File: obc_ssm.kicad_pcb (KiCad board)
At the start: 4 copper layers, 98 x 84 mm, 31 parts, among them IC1 DS3234, J1 RST_JMP, J2 DEBUG CONN, J3 PROGRAMMING PORT, SW1 SW_RST, U1 SN65HVD230, U2 ATMEGA32M1-MU, U3 SST25VF016B, Y1 8MHz

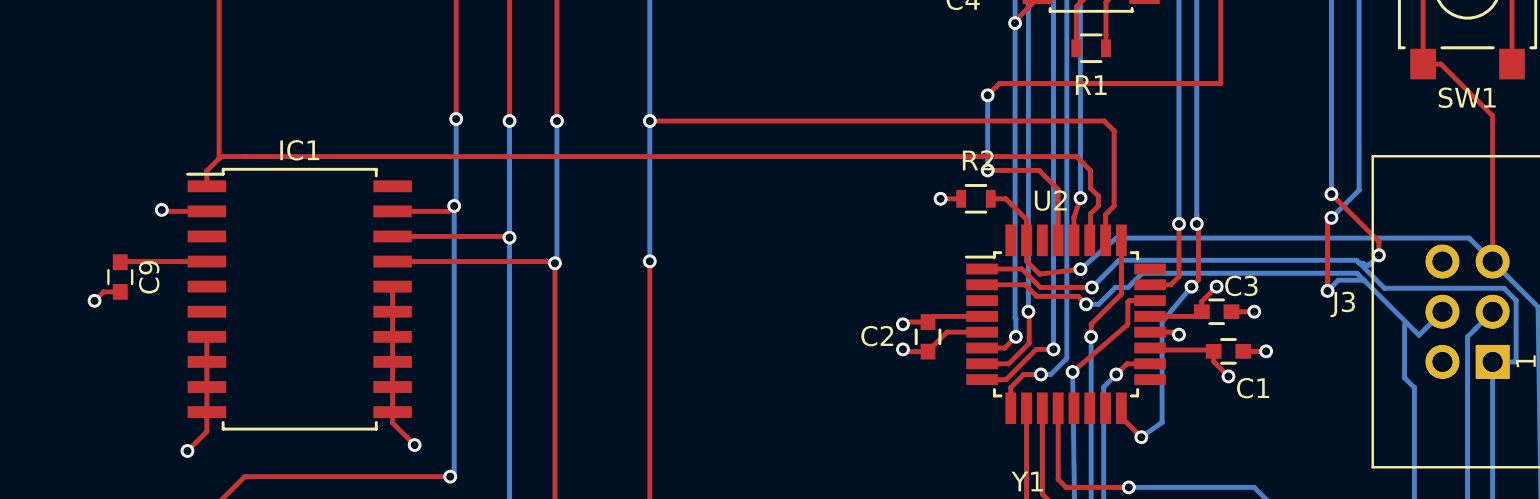
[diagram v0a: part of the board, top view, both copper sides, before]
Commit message: Fix missing connections; DRC check passes
Please review
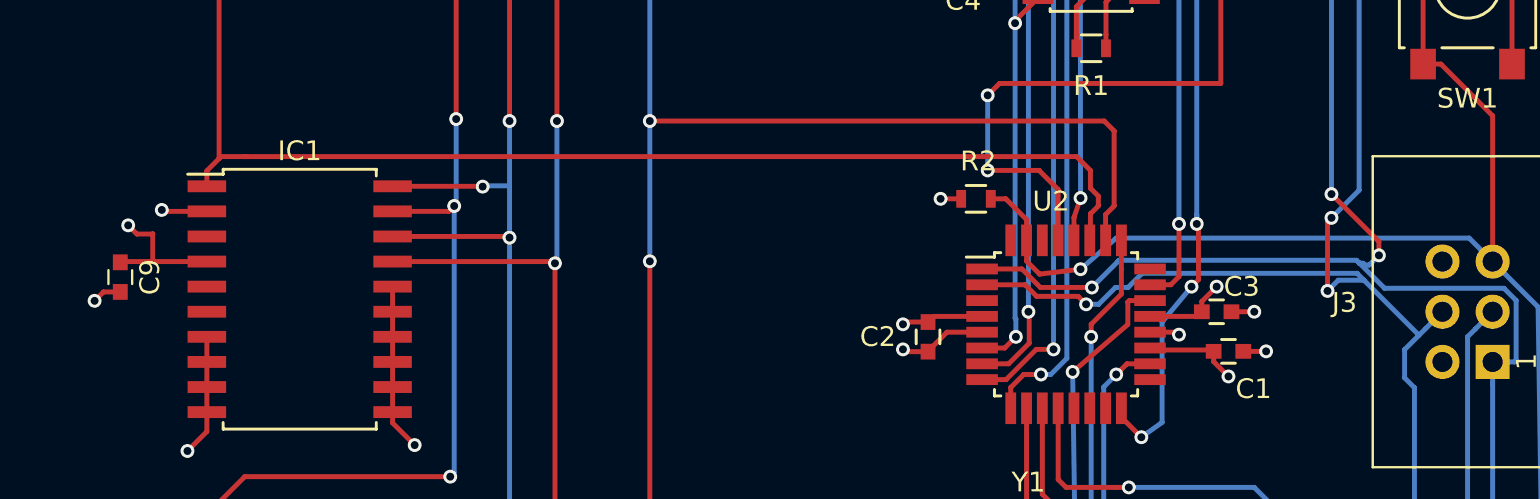
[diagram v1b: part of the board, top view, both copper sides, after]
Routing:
- net /SCK: track 134.4 -> 140.4 mm, vias 5 -> 6
- net +3V3: track 36.3 -> 39.2 mm, vias 9 -> 10
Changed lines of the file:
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@@
   (general
     (links 110)
-    (no_connects 3)
-    (area 99.924999 49.924999 198.075001 134.075001)
+    (no_connects 0)
+    (area 94.1 46.2 221.946906 146.795)
     (thickness 1.6)
     (drawings 61)
-    (tracks 553)
+    (tracks 566)
     (zones 0)
     (modules 31)
@@
   (segment (start 167.862 106.483) (end 169.857 106.483) (width 0.25) (layer F.Cu) (net 1))
   (segment (start 169.857 106.483) (end 170.307 106.033) (width 0.25) (layer F.Cu) (net 1))
+  (segment (start 121.54 89.92) (end 120.74 89.92) (width 0.25) (layer F.Cu) (net 2))
+  (via (at 120.3 89.48) (size 0.7) (drill 0.4) (layers F.Cu B.Cu) (net 2))
+  (segment (start 120.74 89.92) (end 120.3 89.48) (width 0.25) (layer F.Cu) (net 2))
+  (segment (start 121.54 91.313) (end 119.937 91.313) (width 0.25) (layer F.Cu) (net 2))
+  (segment (start 124.2812 91.313) (end 121.54 91.313) (width 0.25) (layer F.Cu) (net 2))
+  (segment (start 121.54 91.313) (end 121.54 89.92) (width 0.25) (layer F.Cu) (net 2))
+  (segment (start 121.54 89.92) (end 121.55 89.91) (width 0.25) (layer F.Cu) (net 2))
   (segment (start 126.7114 110.9258) (end 124.6258 110.9258) (width 0.25) (layer F.Cu) (net 2))
   (via (at 124.6 110.9) (size 0.7) (drill 0.4) (layers F.Cu B.Cu) (net 2))
@@
   (via (at 153 57.2) (size 0.7) (drill 0.4) (layers F.Cu B.Cu) (net 2))
   (segment (start 154.093 58.293) (end 153 57.2) (width 0.25) (layer B.Cu) (net 2))
-  (segment (start 124.2812 91.313) (end 119.937 91.313) (width 0.25) (layer F.Cu) (net 2))
   (segment (start 119.937 91.313) (end 119.9 91.35) (width 0.25) (layer F.Cu) (net 2))
   (segment (start 162.457 88.138) (end 161.417 88.138) (width 0.25) (layer F.Cu) (net 2))
@@
   (segment (start 189.357 108.623998) (end 189.357 97.5066) (width 0.25) (layer B.Cu) (net 39))
   (segment (start 189.357 97.5066) (end 189.357 96.393) (width 0.25) (layer B.Cu) (net 39))
+  (segment (start 184.9 97.2) (end 184.9 95.77) (width 0.25) (layer B.Cu) (net 40))
+  (segment (start 184.9 95.77) (end 185.628399 95.041601) (width 0.25) (layer B.Cu) (net 40))
   (segment (start 185.4 108.1) (end 185.4 97.7) (width 0.25) (layer B.Cu) (net 40))
   (segment (start 185.057499 111.442501) (end 185.6 110.9) (width 0.25) (layer B.Cu) (net 40))
@@
   (segment (start 185.6 108.3) (end 185.4 108.1) (width 0.25) (layer B.Cu) (net 40))
   (segment (start 184.9 111.442501) (end 185.057499 111.442501) (width 0.25) (layer B.Cu) (net 40))
-  (segment (start 184.9 97.2) (end 184.9 94.5) (width 0.25) (layer B.Cu) (net 40))
   (segment (start 185.4 97.7) (end 184.9 97.2) (width 0.25) (layer B.Cu) (net 40))
   (segment (start 185.5 62) (end 184.3 62) (width 0.25) (layer F.Cu) (net 40))
@@
   (segment (start 165.627 97.028) (end 166.497 97.028) (width 0.25) (layer F.Cu) (net 45))
   (via (at 166.497 97.028) (size 0.7) (drill 0.4) (layers F.Cu B.Cu) (net 45))
+  (segment (start 133.6812 87.503) (end 138.223 87.503) (width 0.25) (layer F.Cu) (net 46))
+  (segment (start 138.28 87.48) (end 139.6 87.48) (width 0.25) (layer B.Cu) (net 46))
+  (segment (start 138.24 87.52) (end 138.28 87.48) (width 0.25) (layer B.Cu) (net 46))
+  (via (at 138.24 87.52) (size 0.7) (drill 0.4) (layers F.Cu B.Cu) (net 46))
+  (segment (start 138.223 87.503) (end 138.24 87.52) (width 0.25) (layer F.Cu) (net 46))
   (segment (start 132.1114 110.9258) (end 136.1742 110.9258) (width 0.25) (layer F.Cu) (net 46))
   (segment (start 139.6 107.5) (end 139.6 90.1) (width 0.25) (layer B.Cu) (net 46))
@@
   (segment (start 139.543 90.043) (end 139.6 90.1) (width 0.25) (layer F.Cu) (net 46))
   (via (at 139.6 90.1) (size 0.7) (drill 0.4) (layers F.Cu B.Cu) (net 46))
-  (segment (start 139.6 90.1) (end 139.6 84.2) (width 0.25) (layer B.Cu) (net 46))
+  (segment (start 139.6 90.1) (end 139.6 87.48) (width 0.25) (layer B.Cu) (net 46))
+  (segment (start 139.6 87.48) (end 139.6 84.2) (width 0.25) (layer B.Cu) (net 46))
   (via (at 139.6 84.2) (size 0.7) (drill 0.4) (layers F.Cu B.Cu) (net 46))
   (segment (start 133.6812 90.043) (end 139.543 90.043) (width 0.25) (layer F.Cu) (net 46))
